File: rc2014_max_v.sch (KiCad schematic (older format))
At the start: 11 parts, among them J1 M3 Mounting Hole, J2 Conn_01x40, J4 Conn_01x24, U2 SN74ALVC164245DGG, U3 SN74ALVC164245DGG, U6 SN74ALVC164245DGG

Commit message: fixed errors, connected all pins, switched to 4 layers
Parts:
- removed R10, R11, R12, R13: 10K, Resistor_SMD:R_0603_1608Metric_Pad1.05x0.95mm_HandSolder, symbol Device:R_Small
- removed U2, U3, U6: SN74ALVC164245DGG, Package_SO:TSSOP-48_6.1x12.5mm_P0.5mm, symbol rc2014_max_v-rescue:SN74ALVC164245DGG
- added C1, C10, C11, C12, C13, C14, C2, C3, C4, C5, C6, C7, C8, C9: 100nF, Capacitor_SMD:C_0603_1608Metric_Pad1.05x0.95mm_HandSolder, symbol Device:C
- added R1, R2, R3, R4: 1K, Resistor_SMD:R_0603_1608Metric_Pad1.05x0.95mm_HandSolder, symbol Device:R_Small
- added RN1: 10K, Resistor_SMD:R_Array_Concave_4x0603, symbol Device:R_Pack04
- added U1, U2, U3, U4, U5, U6, U7: TXB0108PWR, Package_SO:TSSOP-20_4.4x6.5mm_P0.65mm, symbol rc2014_max_v-rescue:TXB0108PWR-Logic_LevelTranslator
- renumbered C18 to C15, J4 to J3
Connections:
- net labels added: CLK2_F, OE_C, OE_S, RXA, RXA_F, RXB, RXB_F, TXA, TXA_F, TXB, TXB_F, ~RFSH~_F
- net labels removed: DIR_A, DIR_C_I, DIR_C_O, DIR_D, OE_C_I, OE_C_O, RX_A, RX_A_F, RX_B, TX_A, TX_B, ~RESET2, ~RESET2_F
- wire segments 82 -> 60
- no-connect marks 9 -> 16

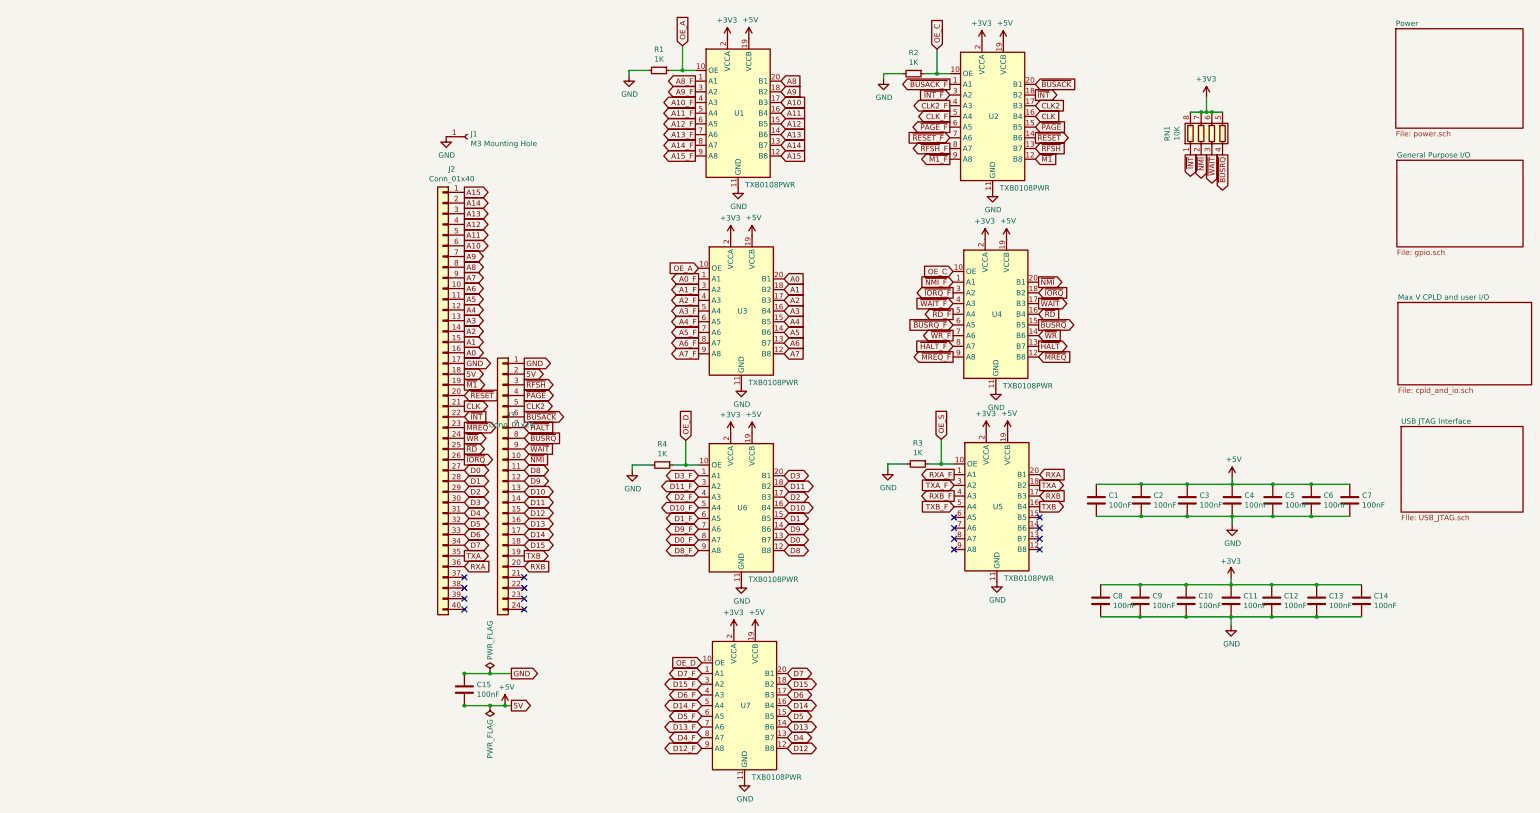
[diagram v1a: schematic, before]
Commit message: consolidated power supply
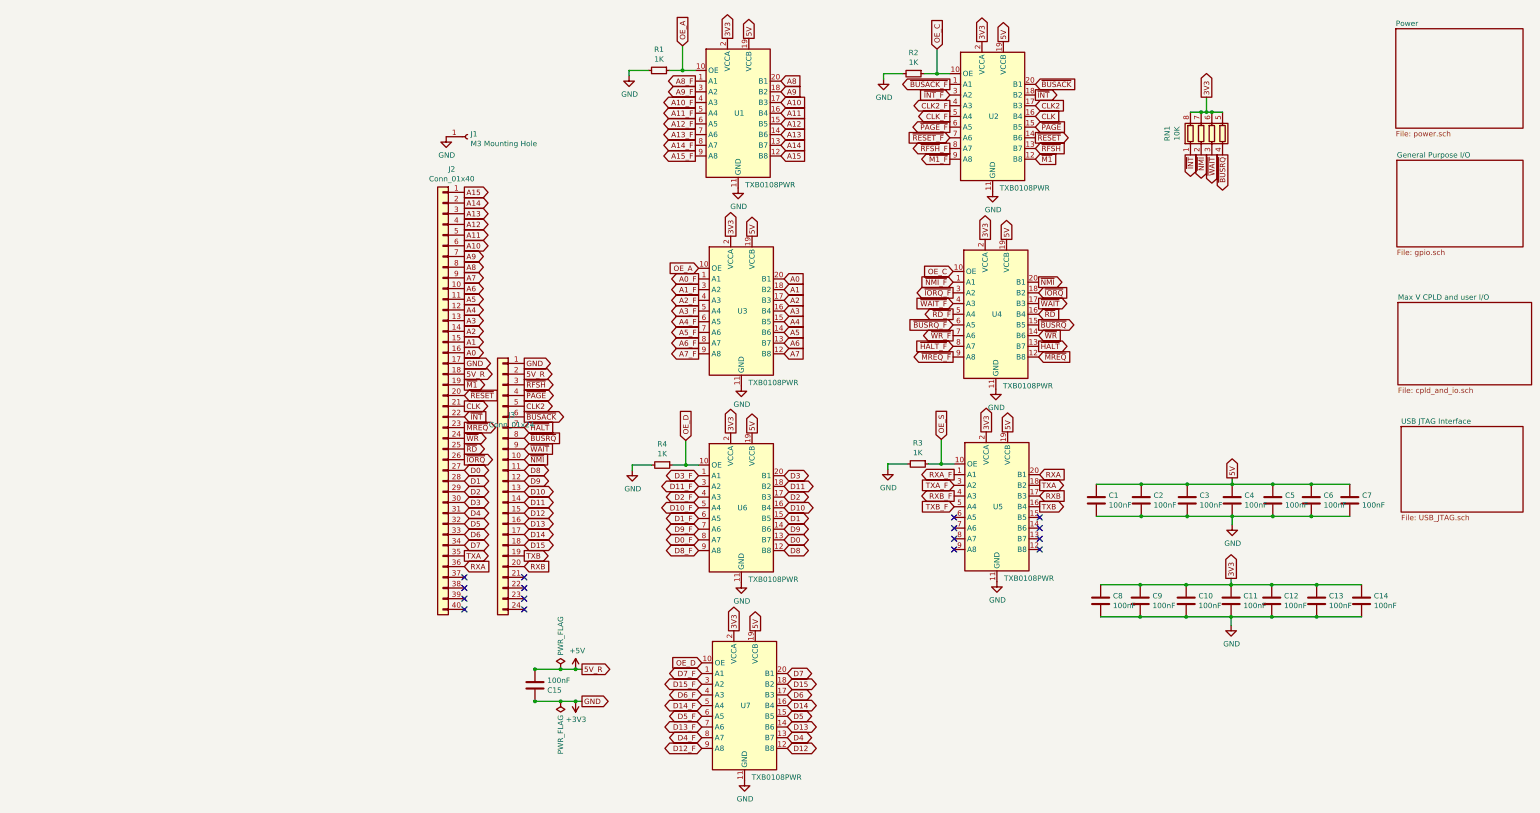
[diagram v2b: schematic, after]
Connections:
- net labels added: 3V3, 5V_R
- wire segments 60 -> 61
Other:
- moved on the sheet: C15

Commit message: Updated BOM
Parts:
- C1, C10, C11, C12, C13, C14, C15, C2, C3, C4, C5, C6, C7, C8, C9: MFR KEMET -> Taiyo Yuden; MPN C0805C104K4RACTU -> TMK107BJ104KA-T; SPN 80-C0805C104K4R -> (none)
- R1, R2, R3, R4: MFR (none) -> Yageo; MPN (none) -> RC0603JR-071KL; SPR (none) -> Mouser
- RN1: MFR (none) -> Panasonic; MPN (none) -> EXB-38V103JV; SPR (none) -> Mouser
- U1, U2, U3, U4, U5, U6, U7: MFR (none) -> Texas Instruments; MPN (none) -> TXB0108PWR; SPR (none) -> Mouser

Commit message: updated descriptions and part #'s
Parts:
- C1, C10, C11, C12, C13, C14, C15, C2, C3, C4, C5, C6, C7, C8, C9: Description (none) -> Multilayer Ceramic Capacitors MLCC - SMD/SMT 0.1uF 25V X5R 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; SPN (none) -> 963-TMK107BJ104KA-T; SPURL https://www.mouser.com/ProductDetail/KEMET/C0805C104K4RACTU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 -> https://www.mouser.com/ProductDetail/963-TMK107BJ104KA-T
- R1, R2, R3, R4: Description (none) -> Thick Film Resistors - SMD 1K OHM 5%; SPN (none) -> 603-RC0603JR-071KL; SPURL (none) -> https://www.mouser.com/ProductDetail/603-RC0603JR-071KL
- RN1: Description (none) -> Resistor Networks & Arrays 10K OHM 5%; SPN (none) -> 667-EXB-38V103JV; SPURL (none) -> https://www.mouser.com/ProductDetail/667-EXB-38V103JV
- U1, U2, U3, U4, U5, U6, U7: Description (none) -> Translation - Voltage Levels 8-Bit Bi-directional V-Level T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; SPN (none) -> 595-TXB0108PWR; SPURL (none) -> https://www.mouser.com/ProductDetail/595-TXB0108PWR

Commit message: parts placement
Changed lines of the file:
@@
 Text GLabel 870  5640 2    50   Input ~ 0
 RXA
-Text GLabel 5440 3680 0    50   Output ~ 0
+Text GLabel 5440 3580 0    50   Output ~ 0
 ~MREQ_F
 Text GLabel 5440 3480 0    50   Output ~ 0
@@
 Text GLabel 3890 7340 2    50   3State ~ 0
 D12
-Text GLabel 6240 3580 2    50   Output ~ 0
+Text GLabel 6240 3680 2    50   Output ~ 0
 ~HALT
 Text GLabel 6240 3380 2    50   Output ~ 0
@@
 Text GLabel 6210 1230 2    50   Output ~ 0
 ~INT
-Text GLabel 6210 1630 2    50   Output ~ 0
+Text GLabel 6210 1530 2    50   Output ~ 0
 ~RESET
 Text GLabel 6210 1130 2    50   Input ~ 0
 ~BUSACK
-Text GLabel 6210 1530 2    50   Input ~ 0
+Text GLabel 6210 1630 2    50   Input ~ 0
 ~PAGE
-Text GLabel 6240 3680 2    50   Input ~ 0
+Text GLabel 6240 3580 2    50   Input ~ 0
 ~MREQ
 Text GLabel 6240 3480 2    50   Input ~ 0
@@
 Text GLabel 6240 3080 2    50   Input ~ 0
 ~IORQ
-Text GLabel 6210 1830 2    50   Input ~ 0
+Text GLabel 6210 1730 2    50   Input ~ 0
 ~M1
-Text GLabel 6210 1430 2    50   Input ~ 0
+Text GLabel 6210 1330 2    50   Input ~ 0
 CLK
 Text GLabel 5440 2980 0    50   Input ~ 0
@@
 Text GLabel 5440 3380 0    50   Input ~ 0
 ~BUSRQ_F
-Text GLabel 5440 3580 0    50   Input ~ 0
+Text GLabel 5440 3680 0    50   Input ~ 0
 ~HALT_F
 Text GLabel 6250 4980 2    50   Input ~ 0
@@
 Text GLabel 5290 800  1    50   Input ~ 0
 OE_C
-Text GLabel 6210 1730 2    50   Input ~ 0
+Text GLabel 6210 1830 2    50   Input ~ 0
 ~RFSH
-Text GLabel 6210 1330 2    50   Input ~ 0
+Text GLabel 6210 1430 2    50   Input ~ 0
 CLK2
 Text GLabel 7960 1790 3    50   Output ~ 0
@@
 Text GLabel 7760 1790 3    50   Output ~ 0
 ~NMI
-Text GLabel 5410 1330 0    50   Output ~ 0
+Text GLabel 5410 1430 0    50   Output ~ 0
 CLK2_F
-Text GLabel 5410 1730 0    50   Output ~ 0
+Text GLabel 5410 1830 0    50   Output ~ 0
 ~RFSH~_F
 Text GLabel 5410 1230 0    50   Input ~ 0
 ~INT_F
-Text GLabel 5410 1630 0    50   Input ~ 0
+Text GLabel 5410 1530 0    50   Input ~ 0
 ~RESET_F
-Text GLabel 5410 1430 0    50   Output ~ 0
+Text GLabel 5410 1330 0    50   Output ~ 0
 CLK_F
-Text GLabel 5410 1830 0    50   Output ~ 0
+Text GLabel 5410 1730 0    50   Output ~ 0
 ~M1_F
-Text GLabel 5410 1530 0    50   Output ~ 0
+Text GLabel 5410 1630 0    50   Output ~ 0
 ~PAGE_F
 Text GLabel 5410 1130 0    50   Output ~ 0

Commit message: started routing
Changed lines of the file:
@@
 Text GLabel 5440 3580 0    50   Output ~ 0
 ~MREQ_F
-Text GLabel 5440 3480 0    50   Output ~ 0
+Text GLabel 5440 3380 0    50   Output ~ 0
 ~WR_F
-Text GLabel 5440 3280 0    50   Output ~ 0
+Text GLabel 5440 3180 0    50   Output ~ 0
 ~RD_F
 Text GLabel 5440 3080 0    50   Output ~ 0
@@
 Text GLabel 6240 3680 2    50   Output ~ 0
 ~HALT
-Text GLabel 6240 3380 2    50   Output ~ 0
+Text GLabel 6240 3480 2    50   Output ~ 0
 ~BUSRQ
-Text GLabel 6240 3180 2    50   Output ~ 0
+Text GLabel 6240 3280 2    50   Output ~ 0
 ~WAIT
 Text GLabel 6240 2980 2    50   Output ~ 0
@@
 Text GLabel 6240 3580 2    50   Input ~ 0
 ~MREQ
-Text GLabel 6240 3480 2    50   Input ~ 0
+Text GLabel 6240 3380 2    50   Input ~ 0
 ~WR
-Text GLabel 6240 3280 2    50   Input ~ 0
+Text GLabel 6240 3180 2    50   Input ~ 0
 ~RD
 Text GLabel 6240 3080 2    50   Input ~ 0
@@
 Text GLabel 5440 2980 0    50   Input ~ 0
 ~NMI_F
-Text GLabel 5440 3180 0    50   Input ~ 0
+Text GLabel 5440 3280 0    50   Input ~ 0
 ~WAIT_F
-Text GLabel 5440 3380 0    50   Input ~ 0
+Text GLabel 5440 3480 0    50   Input ~ 0
 ~BUSRQ_F
 Text GLabel 5440 3680 0    50   Input ~ 0
 ~HALT_F
-Text GLabel 6250 4980 2    50   Input ~ 0
+Text GLabel 6250 4880 2    50   Input ~ 0
 RXB
 Text GLabel 6250 5080 2    50   Output ~ 0
@@
 Text GLabel 6250 4780 2    50   Input ~ 0
 RXA
-Text GLabel 6250 4880 2    50   Output ~ 0
+Text GLabel 6250 4980 2    50   Output ~ 0
 TXA
 Text GLabel 5450 4780 0    50   Output ~ 0
 RXA_F
-Text GLabel 5450 4880 0    50   Input ~ 0
+Text GLabel 5450 4980 0    50   Input ~ 0
 TXA_F
-Text GLabel 5450 4980 0    50   Output ~ 0
+Text GLabel 5450 4880 0    50   Output ~ 0
 RXB_F
 Text GLabel 5450 5080 0    50   Input ~ 0

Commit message: mirror flipped the chips
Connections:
- net labels removed: +3V3
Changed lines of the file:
@@
 	1    0    0    -1
-$EndComp
-$Comp
-L power:+3V3 #PWR?
-U 1 1 5D01DBE0
-P 1910 6900
-AR Path="/5CFABACD/5D01DBE0" Ref="#PWR?"  Part="1"
-AR Path="/5D01DBE0" Ref="#PWR0104"  Part="1"
-AR Path="/5CF9C1ED/5D01DBE0" Ref="#PWR?"  Part="1"
-F 0 "#PWR0104" H 1910 6750 50  0001 C CNN
-F 1 "+3V3" H 1810 7070 50  0000 L CNN
-F 2 "" H 1910 6900 50  0001 C CNN
-F 3 "" H 1910 6900 50  0001 C CNN
-	1    1910 6900
-	-1   0    0    1
 $EndComp
 Text GLabel 1430 3740 2    50   Output ~ 0
@@
 	1520 6600 1530 6600
 Wire Wire Line
-	1770 6900 1910 6900
-Wire Wire Line
 	1530 6900 1770 6900
 Wire Wire Line
@@
 Wire Wire Line
 	1910 6600 1970 6600
-Wire Wire Line
-	1910 6900 1970 6900
 Connection ~ 1770 6600
 Connection ~ 1770 6900
@@
 Connection ~ 8790 5170
 Connection ~ 1910 6600
-Connection ~ 1910 6900
 NoConn ~ 870  5740
 NoConn ~ 870  5840
@@
 NoConn ~ 5450 5280
 NoConn ~ 5450 5180
+Wire Wire Line
+	1770 6900 1905 6900
+$Comp
+L power:GND #PWR0104
+U 1 1 5D17FD05
+P 1905 6900
+AR Path="/5D17FD05" Ref="#PWR0104"  Part="1"
+AR Path="/5CB63856/5D17FD05" Ref="#PWR?"  Part="1"
+AR Path="/5CB5AB00/5CB63856/5D17FD05" Ref="#PWR?"  Part="1"
+AR Path="/5CFABACD/5D17FD05" Ref="#PWR?"  Part="1"
+AR Path="/5CF9C1ED/5D17FD05" Ref="#PWR?"  Part="1"
+F 0 "#PWR0104" H 1905 6650 50  0001 C CNN
+F 1 "GND" H 1910 6727 50  0000 C CNN
+F 2 "" H 1905 6900 50  0001 C CNN
+F 3 "" H 1905 6900 50  0001 C CNN
+	1    1905 6900
+	1    0    0    -1
+$EndComp
+Connection ~ 1905 6900
+Wire Wire Line
+	1905 6900 1970 6900
 $EndSCHEMATC

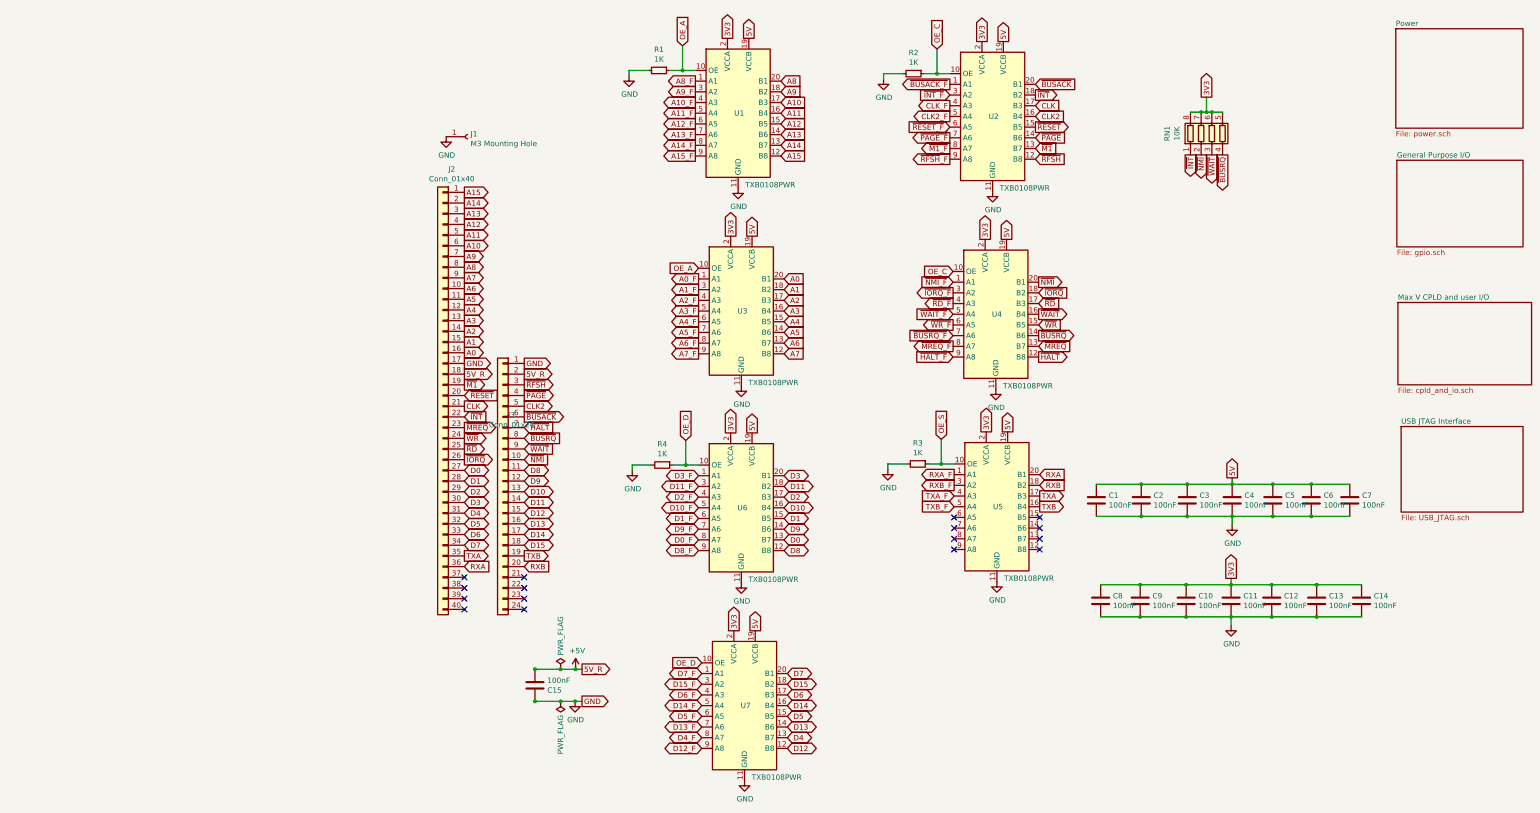
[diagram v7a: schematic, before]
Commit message: moved things around to improve routing, fixed power plane
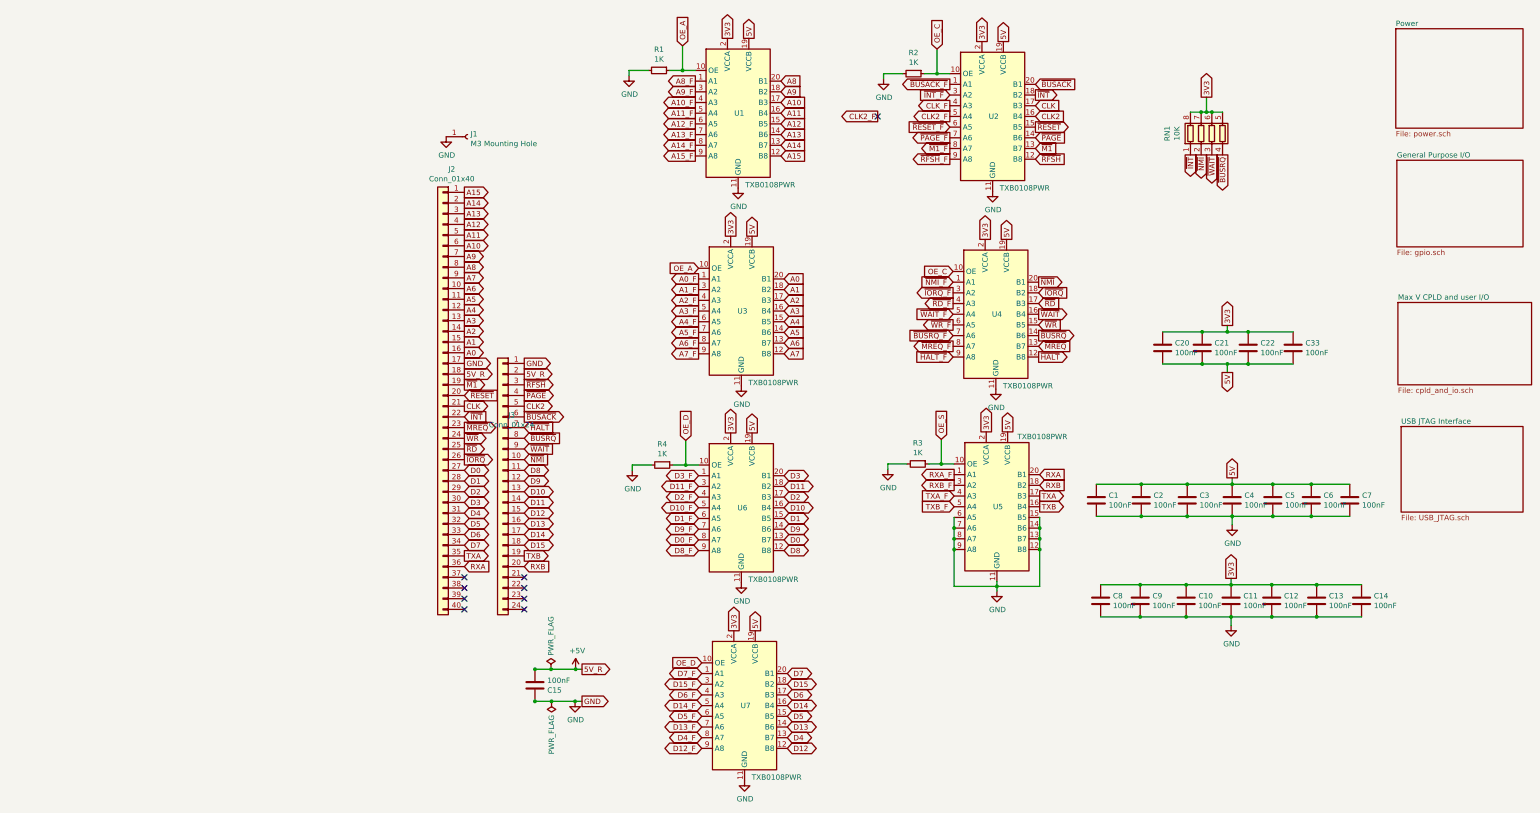
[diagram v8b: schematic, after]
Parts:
- added C20, C21, C22, C33: 100nF, Capacitor_SMD:C_0805_2012Metric_Pad1.15x1.40mm_HandSolder, symbol Device:C
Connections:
- wire segments 61 -> 83
- no-connect marks 16 -> 9
